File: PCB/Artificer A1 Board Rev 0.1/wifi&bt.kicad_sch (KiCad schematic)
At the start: 3 parts

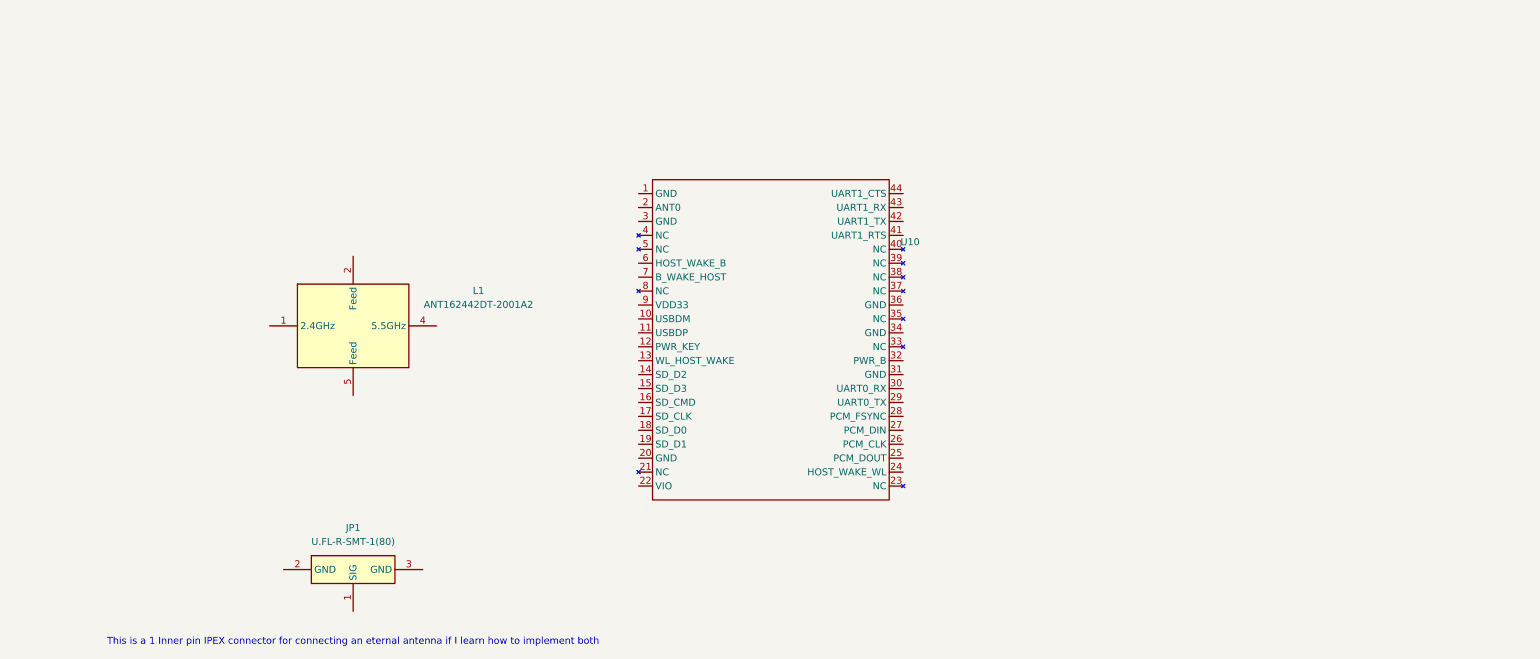
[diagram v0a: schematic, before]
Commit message: added: sd, wifi, audio, started power, fixed buses
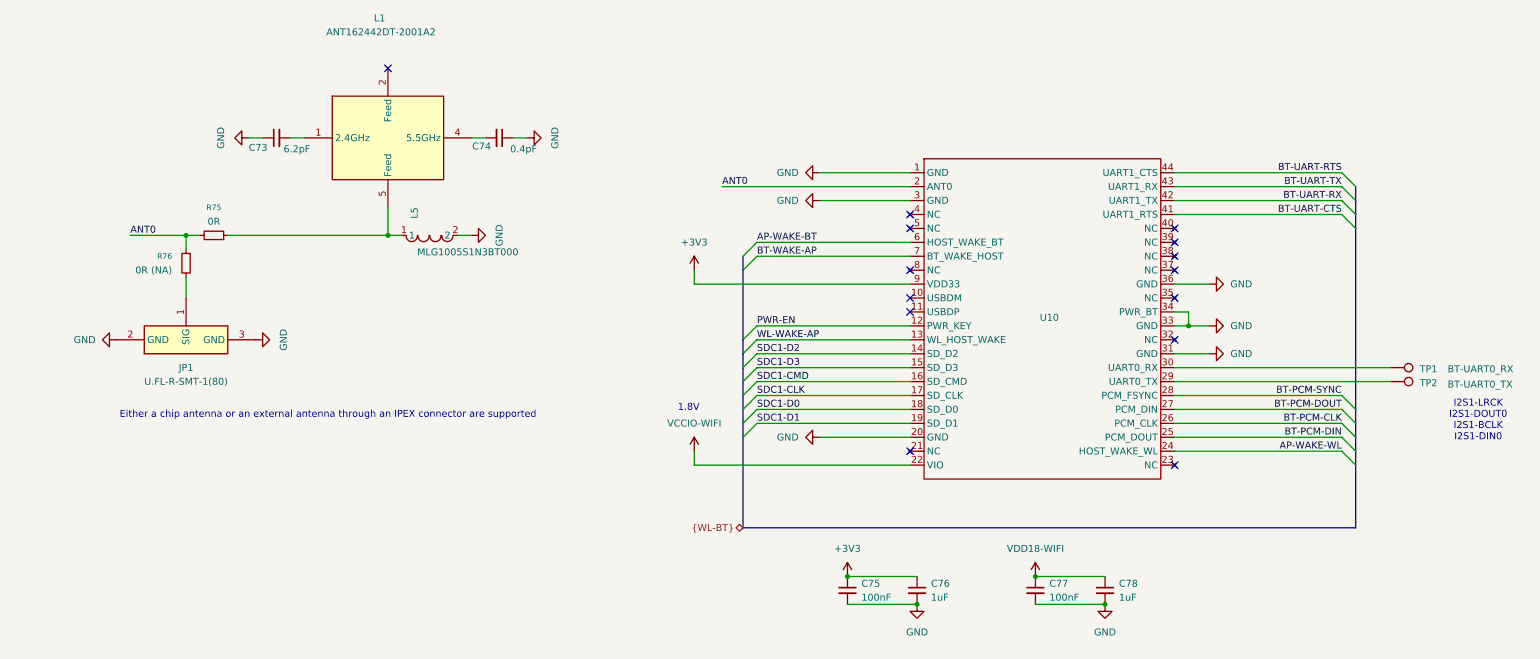
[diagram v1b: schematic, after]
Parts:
- added C73: 6.2pF, symbol Device:C_Small
- added C74: 0.4pF, symbol Device:C_Small
- added C75, C77: 100nF, symbol Device:C_Small
- added C76, C78: 1uF, symbol Device:C_Small
- added L5: MLG1005S1N3BT000, easyeda:L0402, symbol easyeda:MLG1005S1N3BT000
- added R75: 0R, symbol Device:R_Small
- added R76: 0R (NA), symbol Device:R_Small
- added TP1: BT-UART0_RX, symbol Connector:TestPoint
- added TP2: BT-UART0_TX, symbol Connector:TestPoint
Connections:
- net at L1.1 (2.4GHz): now also C73.2
- net at L1.4 (5.5GHz): now also C74.2
- net at L1.5 (Feed): now also L5.1, R75.1
- net GND: now reaches U10.1 (GND)
- net GND: now also JP1.2 (GND), JP1.3 (GND), U10.20 (GND), U10.3 (GND), U10.31 (GND), U10.33 (GND), U10.34 (PWR_BT), U10.36 (GND), C73.1, C74.1, C75.2, C76.2, C77.2, C78.2, L5.2
- net PWR-EN: now reaches U10.12 (PWR_KEY)
- net WL-WAKE-AP: now reaches U10.13 (WL_HOST_WAKE)
- net SDC1-D2: now reaches U10.14 (SD_D2)
- net SDC1-D3: now reaches U10.15 (SD_D3)
- net SDC1-CMD: now reaches U10.16 (SD_CMD)
- net SDC1-CLK: now reaches U10.17 (SD_CLK)
- net SDC1-D0: now reaches U10.18 (SD_D0)
- net SDC1-D1: now reaches U10.19 (SD_D1)
- net ANT0: now reaches U10.2 (ANT0)
- net ANT0: now also R75.2, R76.1
- net VCCIO-WIFI: now reaches U10.22 (VIO)
- net AP-WAKE-WL: now reaches U10.24 (HOST_WAKE_WL)
- net BT-PCM-DIN: now reaches U10.25 (PCM_DOUT)
- net BT-PCM-CLK: now reaches U10.26 (PCM_CLK)
- net BT-PCM-DOUT: now reaches U10.27 (PCM_DIN)
- net BT-PCM-SYNC: now reaches U10.28 (PCM_FSYNC)
- net at U10.29 (UART0_TX): now also TP2.1
- net at U10.30 (UART0_RX): now also TP1.1
- net BT-UART-CTS: now reaches U10.41 (UART1_RTS)
- net BT-UART-RX: now reaches U10.42 (UART1_TX)
- net BT-UART-TX: now reaches U10.43 (UART1_RX)
- net BT-UART-RTS: now reaches U10.44 (UART1_CTS)
- net AP-WAKE-BT: now reaches U10.6 (HOST_WAKE_BT)
- net BT-WAKE-AP: now reaches U10.7 (BT_WAKE_HOST)
- net +3V3: now reaches U10.9 (VDD33)
- net +3V3: now also C75.1, C76.1
- net at JP1.1 (SIG): now also R76.2
- new net VDD18-WIFI: C77.1, C78.1
- no-connect marks 0 -> 14
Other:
- note added: "1.8V"
- note added: "Either a chip antenna or an external antenna through an IPEX connector are supported"
- note added: "I2S1-LRCK I2S1-DOUT0 I2S1-BCLK I2S1-DIN0"
- note removed: "This is a 1 Inner pin IPEX connector for connecting an eternal antenna if I learn how to implement both"
- moved on the sheet: JP1, L1, U10

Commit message: finished rough draft of power supply circuitry!
Yay! This one took a while
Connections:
- net +3V3: no longer U10.9 (VDD33)
- new net VCC33-WIFI: U10.9 (VDD33)
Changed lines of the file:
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@@
+	)
+	(symbol
+		(lib_id "power:+5V")
+		(at 132.08 91.44 0)
+		(unit 1)
+		(exclude_from_sim no)
+		(in_bom yes)
+		(on_board yes)
+		(dnp no)
+		(property "Reference" "#PWR0396"
+			(at 132.08 95.25 0)
+			(effects
+				(font
+					(size 1.27 1.27)
+				)
+				(hide yes)
+			)
+		)
+		(property "Value" "VCC33-WIFI"
+			(at 124.206 89.916 0)
+			(effects
+				(font
+					(size 1.27 1.27)
+				)
+			)
+		)
+		(property "Footprint" ""
+			(at 132.08 91.44 0)
+			(effects
+				(font
+					(size 1.27 1.27)
+				)
+				(hide yes)
+			)
+		)
+		(property "Datasheet" ""
+			(at 132.08 91.44 0)
+			(effects
+				(font
+					(size 1.27 1.27)
+				)
+				(hide yes)
+			)
+		)
+		(property "Description" "Power symbol creates a global label with name \"+5V\""
+			(at 132.08 91.44 0)
+			(effects
+				(font
+					(size 1.27 1.27)
+				)
+				(hide yes)
+			)
+		)
+		(pin "1"
+		)
+		(instances
+			(project "Artificer A1 Board Rev 0.1"
+				(path "/7c37bdb5-94b0-4567-b5ec-a879db855389/bb518e39-315f-4fac-931f-ad14a14e5ca9"
+					(reference "#PWR0396")
+					(unit 1)
+				)
+			)
+		)
 	)
 	(symbol
@@
 					(unit 1)
 				)
-			)
-		)
-	)
-	(symbol
-		(lib_id "power:+3V3")
-		(at 132.08 91.44 0)
-		(unit 1)
-		(exclude_from_sim no)
-		(in_bom yes)
-		(on_board yes)
-		(dnp no)
-		(fields_autoplaced yes)
-		(property "Reference" "#PWR0219"
-			(at 132.08 95.25 0)
-			(effects
-				(font
-					(size 1.27 1.27)
-				)
-				(hide yes)
-			)
-		)
-		(property "Value" "+3V3"
-			(at 132.08 86.36 0)
-			(effects
-				(font
-					(size 1.27 1.27)
-				)
-			)
-		)
-		(property "Footprint" ""
-			(at 132.08 91.44 0)
-			(effects
-				(font
-					(size 1.27 1.27)
-				)
-				(hide yes)
-			)
-		)
-		(property "Datasheet" ""
-			(at 132.08 91.44 0)
-			(effects
-				(font
-					(size 1.27 1.27)
-				)
-				(hide yes)
-			)
-		)
-		(property "Description" "Power symbol creates a global label with name \"+3V3\""
-			(at 132.08 91.44 0)
-			(effects
-				(font
-					(size 1.27 1.27)
-				)
-				(hide yes)
-			)
-		)
-		(pin "1"
-		)
-		(instances
-			(project ""
-				(path "/7c37bdb5-94b0-4567-b5ec-a879db855389/bb518e39-315f-4fac-931f-ad14a14e5ca9"
-					(reference "#PWR0219")
-					(unit 1)
-				)
